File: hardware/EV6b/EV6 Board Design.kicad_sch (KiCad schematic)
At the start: 110 parts, among them J1 Conn_01x02_Female, J10 Conn_01x08_Female, J11 Conn_01x06_Female, J12 Conn_01x04_Female, J13 Conn_01x04_Female, J14 Conn_01x04_Female, J15 Conn_01x02_Female, J2 Conn_01x02_Female, J3 Conn_01x04_Female, J4 Conn_01x08_Male, J5 Conn_01x04_Female, J6 Conn_01x04_Female, J7 Conn_01x04_Female, J8 Conn_01x06_Female, J9 USB_C_Receptacle, SW1 SW_Push, SW2 SW_Push, SW3 SW_Push, U1 STM32F405RGTx, U11 ESP32-S3-WROOM-1-N8R2, U12 MCP73832-2-OT, U13 BM14B(0.8)-24DS-0.4V(53), U2 AMS1117-3.3, U3 CH340C, U4 USBLC6-2P6, U5 STM32F030C8Tx, U6 WM8960CGEFL/RV, Y1 Crystal_GND24

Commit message: mods for EV6b schematic and pcb
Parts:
- U5: value STM32F030C8Tx -> STM32F091CCT6
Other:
- title: EV6 - FINN BERG -> EV6b - FINN BERG

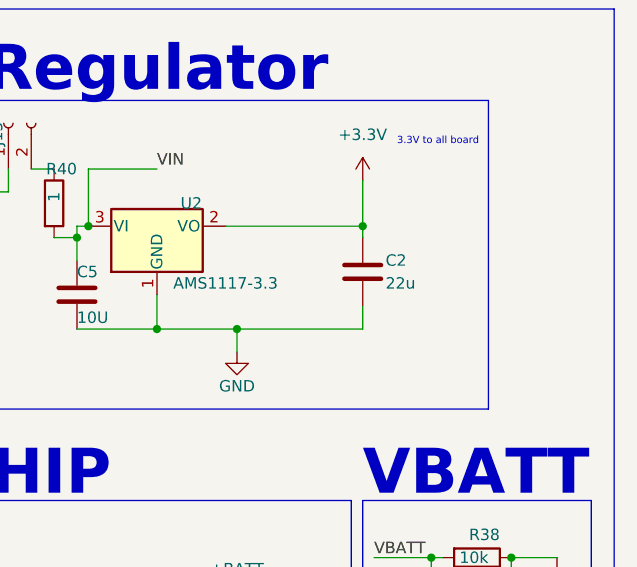
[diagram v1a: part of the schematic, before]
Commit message: update BOM with change 20 to 15u Cap
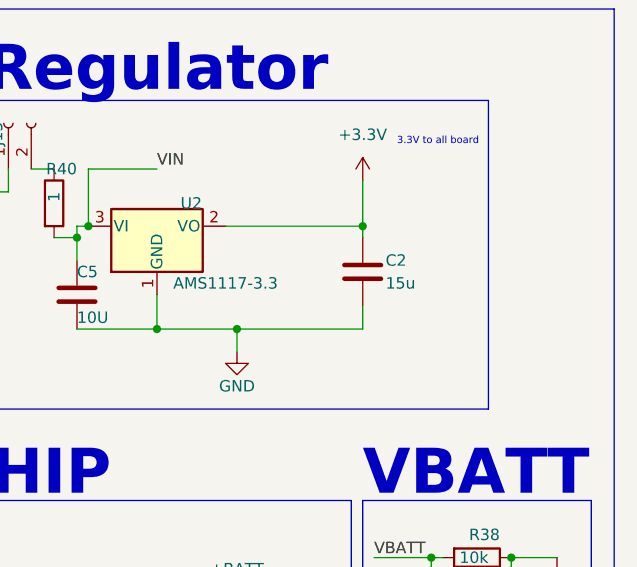
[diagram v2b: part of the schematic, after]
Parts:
- C2: value 22u -> 15u
- U13: footprint BM14B(0.B)-24DS-0:BM14B(0.B)-24DS-0.4V(53) -> (none)
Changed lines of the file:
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@@
       (effects (font (size 1.27 1.27)) (justify left))
     )
-    (property "Value" "22u" (at 525.78 55.88 0)
+    (property "Value" "15u" (at 525.78 55.88 0)
       (effects (font (size 1.27 1.27)) (justify left))
     )
@@
       (effects (font (size 1.27 1.27)) (justify left))
     )
-    (property "Footprint" "BM14B(0.B)-24DS-0:BM14B(0.B)-24DS-0.4V(53)" (at 495.3 217.17 0)
+    (property "Footprint" "" (at 495.3 217.17 0)
       (effects (font (size 1.27 1.27)) hide)
     )

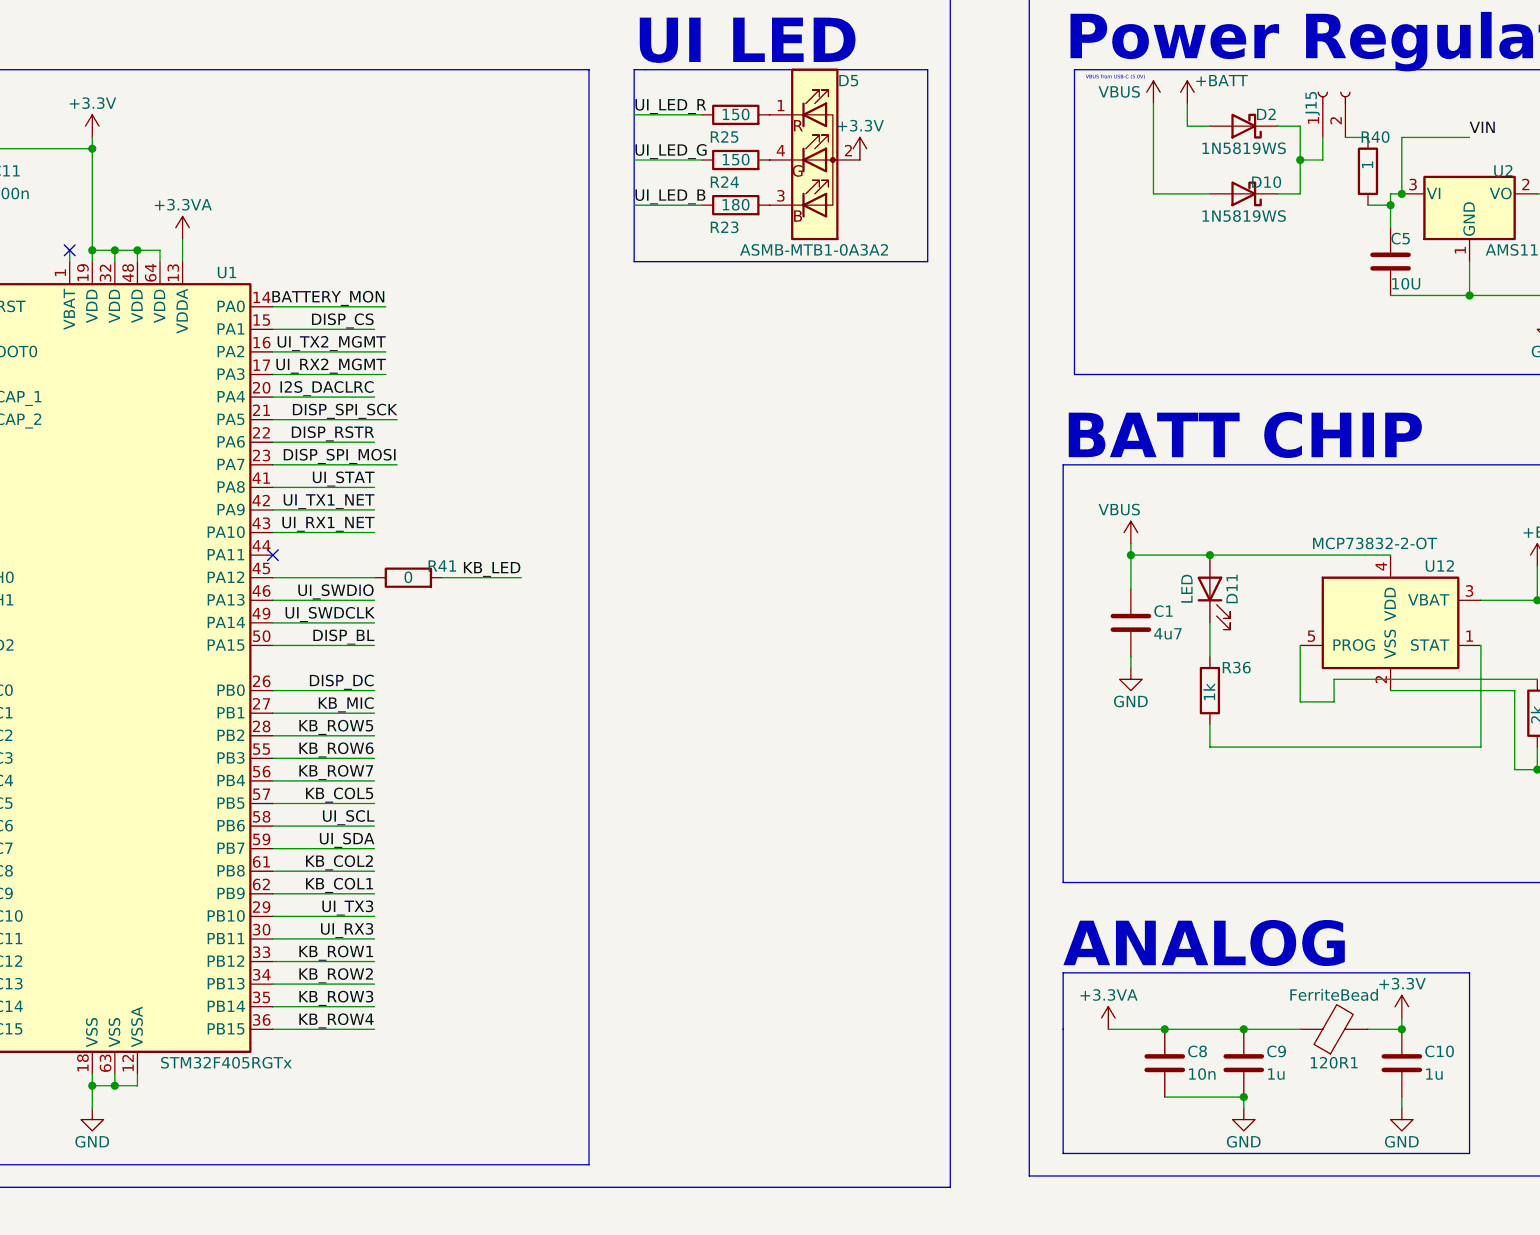
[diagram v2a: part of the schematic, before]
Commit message: Move to STM32F446
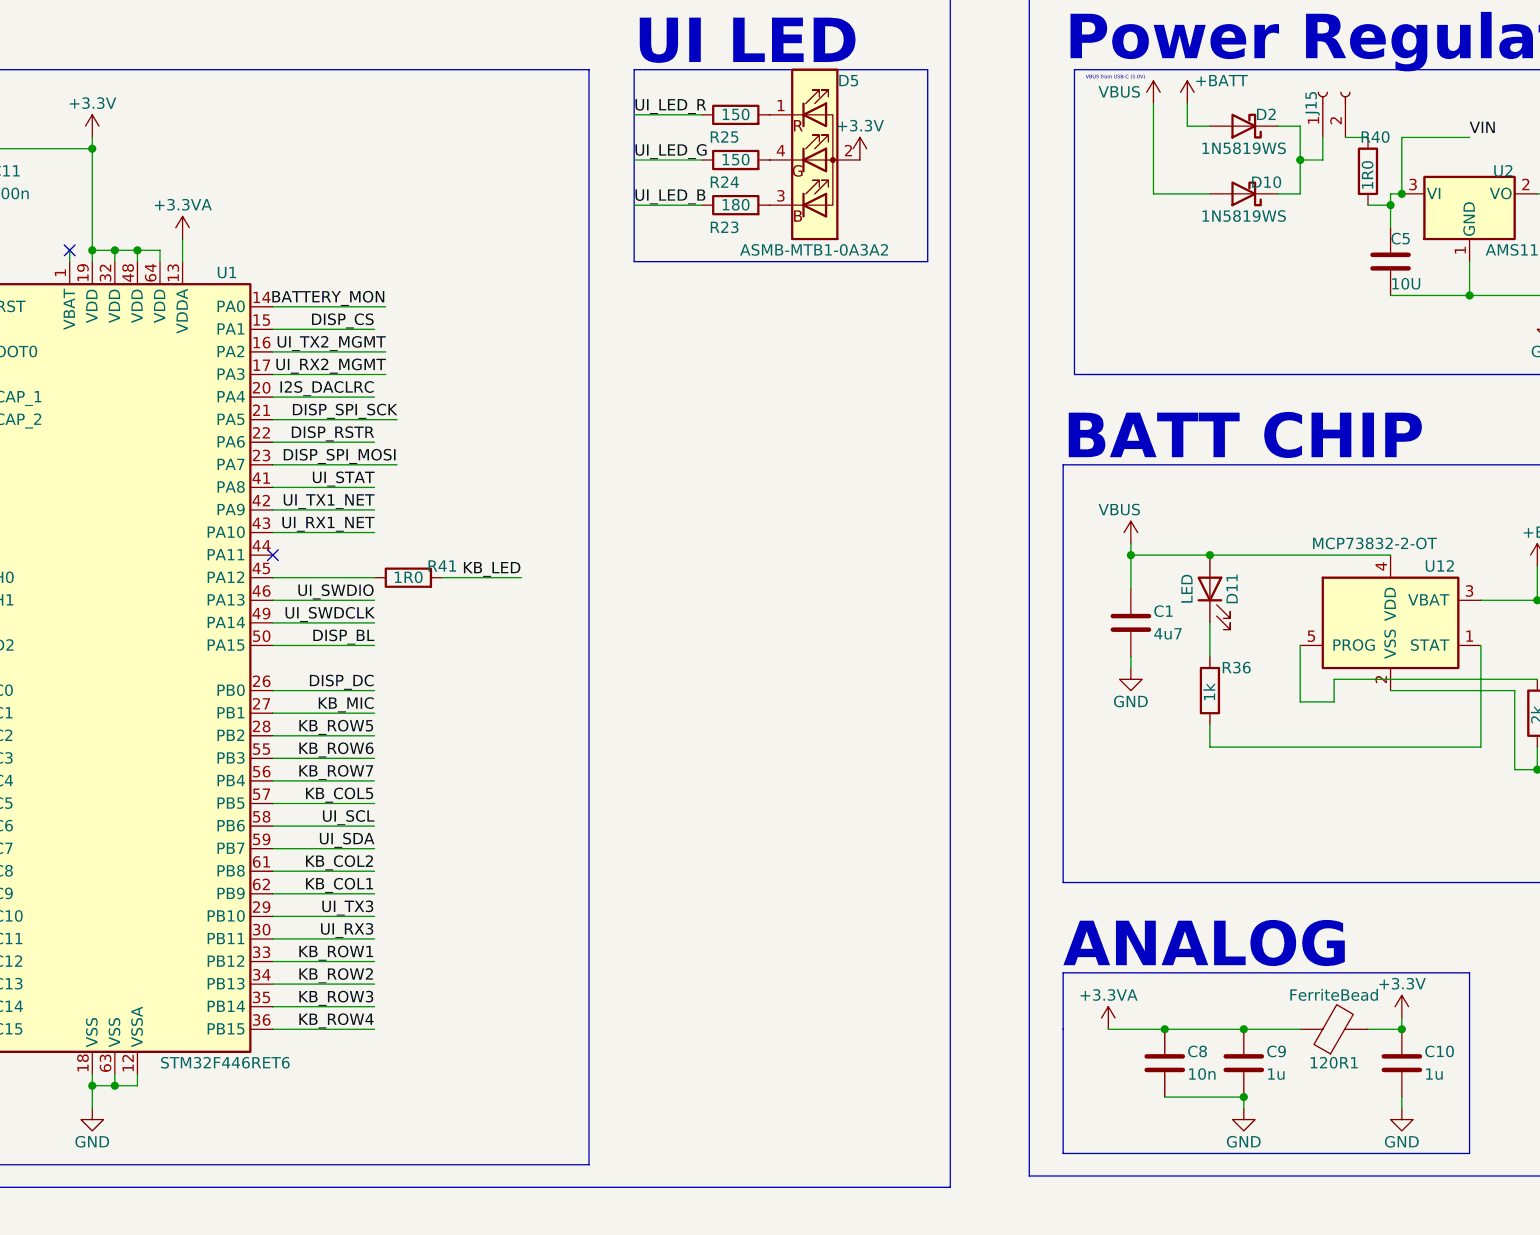
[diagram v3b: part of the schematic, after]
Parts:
- R40: value 1 -> 1R0
- R41: value 0 -> 1R0
- U1: value STM32F405RGTx -> STM32F446RET6
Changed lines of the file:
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@@
       (effects (font (size 1.27 1.27)))
     )
-    (property "Value" "0" (at 381 92.71 90)
+    (property "Value" "1R0" (at 381 92.71 90)
       (effects (font (size 1.27 1.27)))
     )
@@
       (effects (font (size 1.27 1.27)) (justify right))
     )
-    (property "Value" "1" (at 488.95 45.72 90)
+    (property "Value" "1R0" (at 488.95 45.72 90)
       (effects (font (size 1.27 1.27)) (justify right))
     )
@@
       (effects (font (size 1.27 1.27)) (justify left))
     )
-    (property "Value" "STM32F405RGTx" (at 353.06 147.32 0)
-      (effects (font (size 1.27 1.27)) (justify left))
-    )
+    (property "Value" "STM32F446RET6" (at 353.06 147.32 0)
+      (effects (font (size 1.27 1.27)) (justify left))
+    )

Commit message: updates for next rev
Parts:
- J10, U13, U6: now not fitted
- U5: LCSC (none) -> C129795
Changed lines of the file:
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@@
   )
   (symbol (lib_name "WM8960CGEFL{slash}RV_1") (lib_id "Audio Interface:WM8960CGEFL{slash}RV") (at 207.01 205.74 0) (unit 1)
-    (in_bom yes) (on_board yes) (dnp no) (fields_autoplaced)
+    (in_bom yes) (on_board yes) (dnp yes) (fields_autoplaced)
     (property "Reference" "U6" (at 228.6 154.94 0)
       (effects (font (size 1.27 1.27)))
@@
       (effects (font (size 1.27 1.27)) hide)
     )
+    (property "LCSC" "" (at 207.01 205.74 0)
+      (effects (font (size 1.27 1.27)) hide)
+    )
     (pin "1")
     (pin "10")
@@
   )
   (symbol (lib_id "Keyboard Symbol:BM14B(0.8)-24DS-0.4V(53)") (at 491.49 212.09 0) (unit 1)
-    (in_bom yes) (on_board yes) (dnp no)
+    (in_bom yes) (on_board yes) (dnp yes)
     (property "Reference" "U13" (at 497.84 180.34 0)
       (effects (font (size 1.27 1.27)) (justify left))
@@
       (effects (font (size 1.27 1.27)) hide)
     )
+    (property "LCSC" "C129795" (at 82.55 92.71 0)
+      (effects (font (size 1.27 1.27)) hide)
+    )
     (pin "1")
     (pin "10")
@@
   )
   (symbol (lib_id "Connector:Conn_01x08_Female") (at 342.9 255.27 0) (unit 1)
-    (in_bom yes) (on_board yes) (dnp no)
+    (in_bom yes) (on_board yes) (dnp yes)
     (property "Reference" "J10" (at 341.63 246.38 0)
       (effects (font (size 1.27 1.27)) (justify left))
